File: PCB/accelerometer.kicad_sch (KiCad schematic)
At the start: 4 parts

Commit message: fix: latch gate-drive divider, floating buck EN, and missing accelerometer MPNs (#58)
Power latch, round 2 (found via cross-checking a third-party static-analysis
tool run against this project's own netlist and real component datasheets):

- R_LATCH_G1 raised 10kΩ -> 1MΩ. The prior value formed an unintended divider
  with R_INV_PU1 across D_OR1, leaving only ~0.3V at Q_LATCH1's gate on a
  press -- nowhere near enough to turn it on, meaning last round's inverter
  fix likely didn't actually latch on real hardware. Raising the pull-down
  instead of shrinking the pull-up avoids turning Q_INV1's idle state into a
  continuous mA-scale drain.
- R_INV_BASE1 repurposed from a series resistor (which shared current with
  R_BTN_PU1 and sagged the MCU's own button-sense read to ~1V) into its own
  dedicated 100k VSYS pull-up, decoupled via a new Schottky (D_INV_ISO1,
  BAT54W) so a press can still pull the base low without loading the shared
  sense node.
- Added R_PWR_EN_PD1 (100k to GND): the buck's EN pin had no pull-up or
  pull-down at all. TI's TLV62569 datasheet says not to leave it floating;
  Q_PWR1's drain is its only prior connection.

Also fills in MF/MPN for the 4 accelerometer parts (U_ACCEL1, C_ACCEL_1/2/3)
that were missing them, and retires the JLCPCB Basic-library matching
preference -- we're no longer targeting JLCPCB assembly for this board.

power_control_layout diagrams updated to match. Verified via kicad-cli sch
erc, sch export netlist, and pcb drc after every change; production files
regenerated.

Co-authored-by: Claude Sonnet 5 <noreply@anthropic.com>
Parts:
- C_ACCEL_1: LCSC (none) -> C15195; MF (none) -> Samsung Electro-Mechanics; Manufacturer_Part_Number (none) -> CL05B103KB5NNNC
- C_ACCEL_2: LCSC (none) -> C1546; MF (none) -> FH (Guangdong Fenghua Advanced Tech); Manufacturer_Part_Number (none) -> 0402CG101J500NT
- C_ACCEL_3: LCSC (none) -> C84703; MF (none) -> Samsung Electro-Mechanics; Manufacturer_Part_Number (none) -> CL05B222KB5NNNC
- U_ACCEL1: LCSC (none) -> C2887190; MF (none) -> QST; Manufacturer_Part_Number (none) -> QMA6100P
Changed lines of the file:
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@@
+			)
+		)
+		(property "MF" "Samsung Electro-Mechanics"
+			(at 0 0 0)
+			(hide yes)
+			(show_name no)
+			(do_not_autoplace no)
+			(effects
+				(font
+					(size 1.27 1.27)
+				)
+			)
+		)
+		(property "Manufacturer_Part_Number" "CL05B103KB5NNNC"
+			(at 0 0 0)
+			(hide yes)
+			(show_name no)
+			(do_not_autoplace no)
+			(effects
+				(font
+					(size 1.27 1.27)
+				)
+			)
+		)
+		(property "LCSC" "C15195"
+			(at 0 0 0)
+			(hide yes)
+			(show_name no)
+			(do_not_autoplace no)
+			(effects
+				(font
+					(size 1.27 1.27)
+				)
 			)
 		)
@@
 			)
 		)
+		(property "MF" "QST"
+			(at 0 0 0)
+			(hide yes)
+			(show_name no)
+			(do_not_autoplace no)
+			(effects
+				(font
+					(size 1.27 1.27)
+				)
+			)
+		)
+		(property "Manufacturer_Part_Number" "QMA6100P"
+			(at 0 0 0)
+			(hide yes)
+			(show_name no)
+			(do_not_autoplace no)
+			(effects
+				(font
+					(size 1.27 1.27)
+				)
+			)
+		)
+		(property "LCSC" "C2887190"
+			(at 0 0 0)
+			(hide yes)
+			(show_name no)
+			(do_not_autoplace no)
+			(effects
+				(font
+					(size 1.27 1.27)
+				)
+			)
+		)
 		(pin "1"
 		)
@@
 			)
 		)
+		(property "MF" "FH (Guangdong Fenghua Advanced Tech)"
+			(at 0 0 0)
+			(hide yes)
+			(show_name no)
+			(do_not_autoplace no)
+			(effects
+				(font
+					(size 1.27 1.27)
+				)
+			)
+		)
+		(property "Manufacturer_Part_Number" "0402CG101J500NT"
+			(at 0 0 0)
+			(hide yes)
+			(show_name no)
+			(do_not_autoplace no)
+			(effects
+				(font
+					(size 1.27 1.27)
+				)
+			)
+		)
+		(property "LCSC" "C1546"
+			(at 0 0 0)
+			(hide yes)
+			(show_name no)
+			(do_not_autoplace no)
+			(effects
+				(font
+					(size 1.27 1.27)
+				)
+			)
+		)
 		(pin "1"
 		)
@@
 			(show_name no)
 			(do_not_autoplace no)
+			(effects
+				(font
+					(size 1.27 1.27)
+				)
+			)
+		)
+		(property "MF" "Samsung Electro-Mechanics"
+			(at 0 0 0)
+			(hide yes)
+			(show_name no)
+			(do_not_autoplace no)
+			(effects
+				(font
+					(size 1.27 1.27)
+				)
+			)
+		)
+		(property "Manufacturer_Part_Number" "CL05B222KB5NNNC"
+			(at 0 0 0)
+			(hide yes)
+			(show_name no)
+			(do_not_autoplace no)
+			(effects
+				(font
+					(size 1.27 1.27)
+				)
+			)
+		)
+		(property "LCSC" "C84703"
+			(at 0 0 0)
+			(hide yes)
+			(show_name no)
+			(do_not_autoplace no)

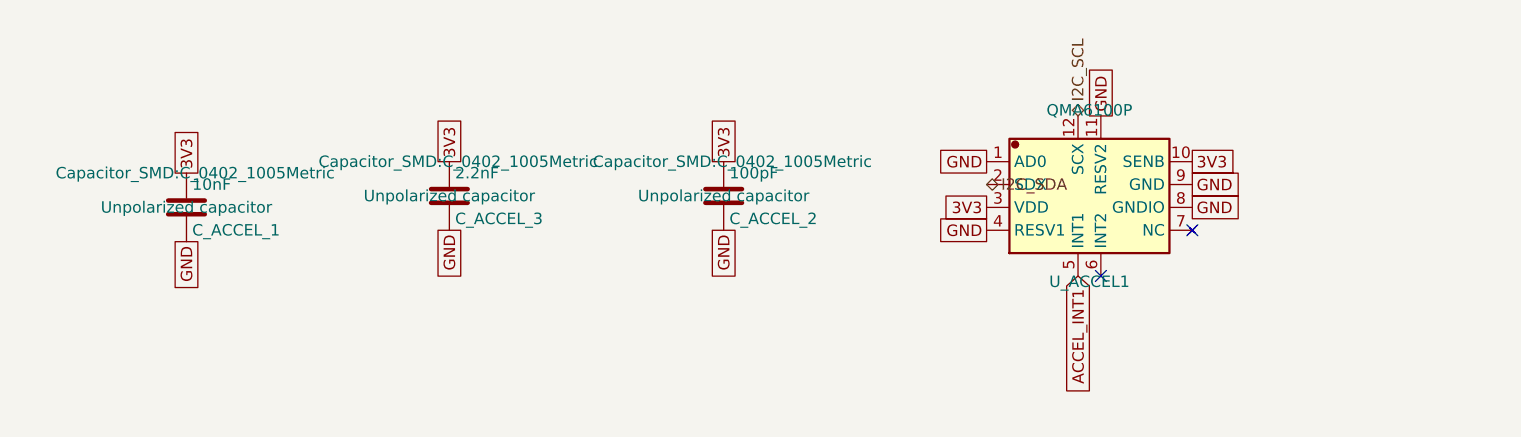
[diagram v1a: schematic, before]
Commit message: fix: make every BOM Value unambiguous for the fab, and switch D_INV_ISO1 to SOT-323 (#61)
* fix: make every BOM Value unambiguous for the fab, and switch D_INV_ISO1 to SOT-323

PCBWay flagged D_INV_ISO1: "BAT54W" is SOT-323 from nearly every maker, but we
had picked Yangjie's SOD-123 variant. A fab only sees Designator, Footprint,
Quantity and Value in the BOM (never MF/MPN/LCSC), so a bare part name is
ambiguous. Fixes the class of problem, not just this part:

- Every component's Value is now "<label> | <MPN> | <manufacturer> | <package>"
  (label dropped when it repeats the MPN; commas/periods stripped so the CSV
  never needs quoting). BT1 keeps its RIGHT-ANGLE HORIZONTAL note. Applied to
  all 81 parts across every sheet and the PCB.
- scripts/bom_values.py builds, applies, and checks these values, including
  that the PCB copy of Value/MF/MPN/footprint matches the schematic. New
  footprints must be added to its package table on purpose; hand-sourced parts
  with no MPN (J_STICK1) are listed explicitly.
- D_INV_ISO1 -> Diodes BAT54W-7-F in SOT-323 (common part, several makers).
  Pin 1 anode / pin 2 not connected / pin 3 cathode, confirmed against
  Nexperia's numbered pinning table and Diodes' datasheet. Uses KiCad's
  Diode:BAT54W symbol; PCB footprint replaced and rerouted. Electrically the
  same BAT54 family (30V, 200mA, 2uA leakage at 25V), so the SPICE model and
  scripts/spice/latch_sim.py still pass.
- Layout diagrams now say AO3401A for Q_PWR1 (they were stale since it was
  swapped from DMG2305UX) and BAT54W-7-F/SOT-323 for D_INV_ISO1.
- Repo CLAUDE.md documents the Value rule and the script.

ERC/DRC clean; production files regenerated.

Co-Authored-By: Claude Sonnet 5 <noreply@anthropic.com>

* chore: commit KiCad project settings (reordered used-designators list)

Co-Authored-By: Claude Sonnet 5 <noreply@anthropic.com>

---------

Co-authored-by: Claude Sonnet 5 <noreply@anthropic.com>
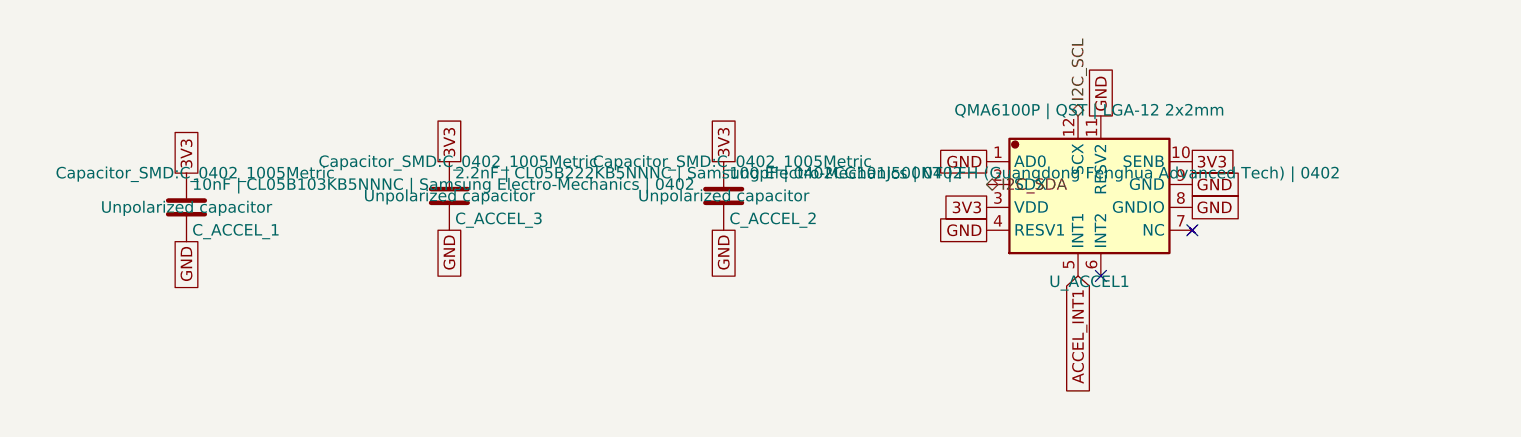
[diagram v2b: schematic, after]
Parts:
- C_ACCEL_1: value 10nF -> 10nF | CL05B103KB5NNNC | Samsung Electro-Mechanics | 0402
- C_ACCEL_2: value 100pF -> 100pF | 0402CG101J500NT | FH (Guangdong Fenghua Advanced Tech) | 0402
- C_ACCEL_3: value 2.2nF -> 2.2nF | CL05B222KB5NNNC | Samsung Electro-Mechanics | 0402
- U_ACCEL1: value QMA6100P -> QMA6100P | QST | LGA-12 2x2mm
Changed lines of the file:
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@@
 			)
 		)
-		(property "Value" "10nF"
+		(property "Value" "10nF | CL05B103KB5NNNC | Samsung Electro-Mechanics | 0402"
 			(at 98.425 102.87 0)
 			(show_name no)
@@
 			)
 		)
-		(property "Value" "QMA6100P"
+		(property "Value" "QMA6100P | QST | LGA-12 2x2mm"
 			(at 198.12 94.615 0)
 			(show_name no)
@@
 			)
 		)
-		(property "Value" "100pF"
+		(property "Value" "100pF | 0402CG101J500NT | FH (Guangdong Fenghua Advanced Tech) | 0402"
 			(at 158.115 101.6 0)
 			(show_name no)
@@
 			)
 		)
-		(property "Value" "2.2nF"
+		(property "Value" "2.2nF | CL05B222KB5NNNC | Samsung Electro-Mechanics | 0402"
 			(at 127.635 101.6 0)
 			(show_name no)
